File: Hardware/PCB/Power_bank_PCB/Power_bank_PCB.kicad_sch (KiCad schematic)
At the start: 96 parts, among them IC1 TPS63070RNMR, IC2 TPS63070RNMR, J1 Alterative_charging, J2 Vout, Q1 2N7002, Q2 8205A, Q3 2N7002, Q4 2N7002, Q5 2N7002, Q6 DMP3099L, U1 TP4056-42-ESOP8, U2 MCP4018-10k, U3 DW01A, U4 TPS61022, U5 STM32U031F8Px, U6 INA219AxD

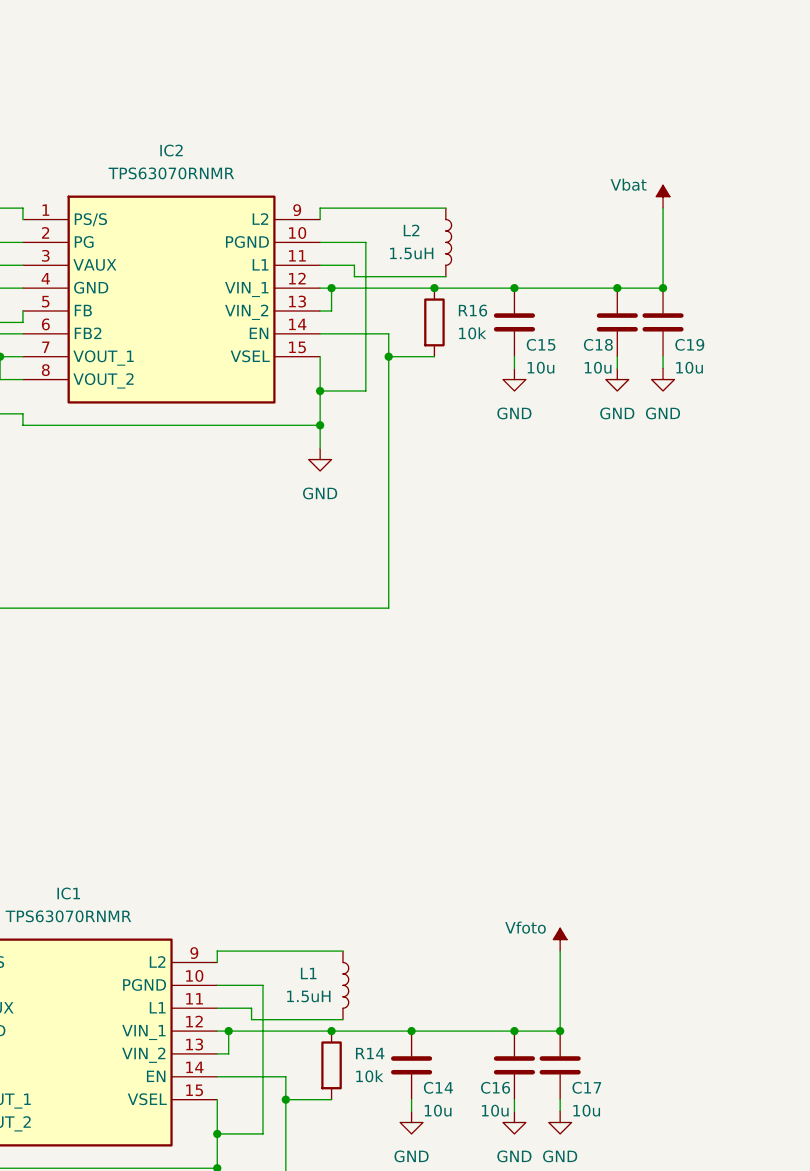
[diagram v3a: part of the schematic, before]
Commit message: First layout without traces
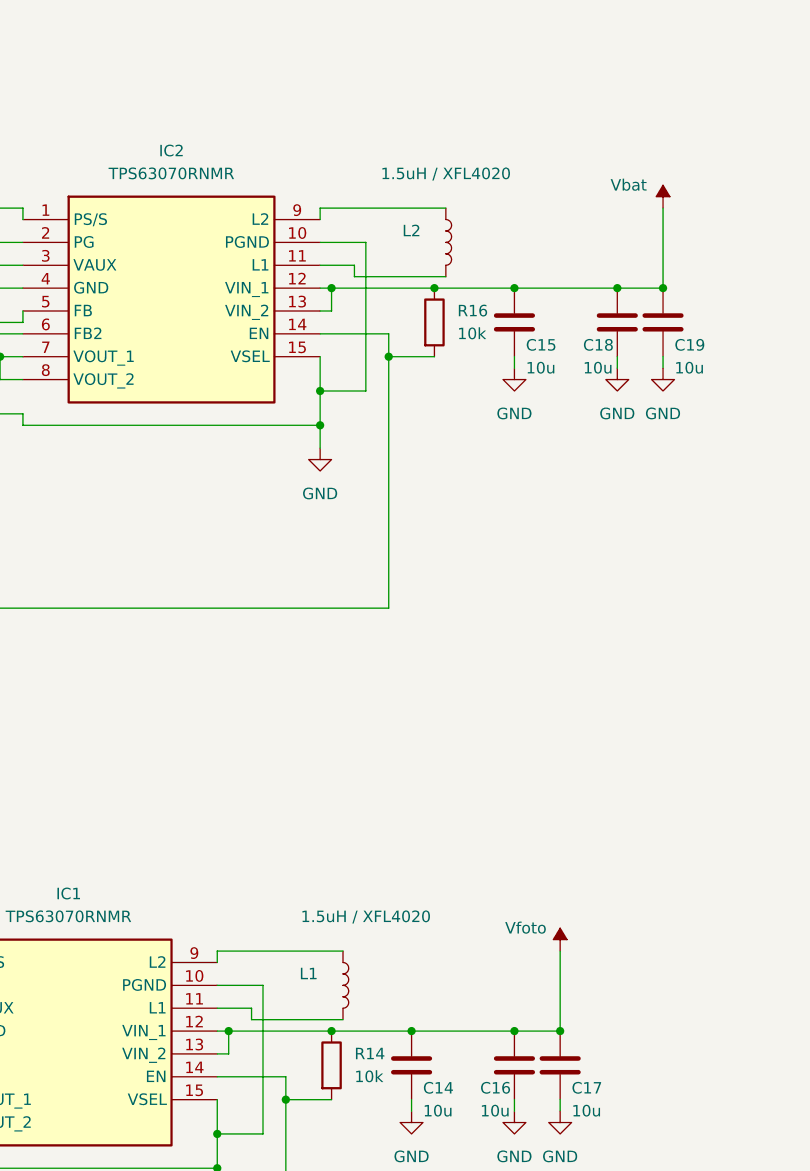
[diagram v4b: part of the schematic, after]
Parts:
- L1, L2: value 1.5uH -> 1.5uH / XFL4020; footprint (none) -> Inductor_SMD:L_Coilcraft_XAL4020-XXX
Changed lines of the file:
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@@
 			)
 		)
-		(property "Value" "1.5uH"
-			(at 139.7 153.67 0)
-			(show_name no)
-			(do_not_autoplace no)
-			(effects
-				(font
-					(size 1.27 1.27)
-				)
-			)
-		)
-		(property "Footprint" ""
+		(property "Value" "1.5uH / XFL4020"
+			(at 143.51 144.78 0)
+			(show_name no)
+			(do_not_autoplace no)
+			(effects
+				(font
+					(size 1.27 1.27)
+				)
+			)
+		)
+		(property "Footprint" "Inductor_SMD:L_Coilcraft_XAL4020-XXX"
 			(at 143.51 152.4 0)
 			(hide yes)
@@
 			)
 		)
-		(property "Value" "1.5uH"
-			(at 128.27 236.22 0)
-			(show_name no)
-			(do_not_autoplace no)
-			(effects
-				(font
-					(size 1.27 1.27)
-				)
-			)
-		)
-		(property "Footprint" ""
+		(property "Value" "1.5uH / XFL4020"
+			(at 134.62 227.33 0)
+			(show_name no)
+			(do_not_autoplace no)
+			(effects
+				(font
+					(size 1.27 1.27)
+				)
+			)
+		)
+		(property "Footprint" "Inductor_SMD:L_Coilcraft_XAL4020-XXX"
 			(at 132.08 234.95 0)
 			(hide yes)

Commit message: Positioned modules on PCB and created zones
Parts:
- TP1, TP10, TP11, TP12, TP2, TP3, TP4, TP5, TP6, TP7, TP8, TP9: footprint TestPoint:TestPoint_Pad_D4.0mm -> TestPoint:TestPoint_Pad_D2.0mm
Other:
- company: (none) -> Bart Soul
- title: (none) -> SolarBank
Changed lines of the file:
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@@
 	(generator_version "10.0")
 	(paper "A3")
+	(title_block
+		(title "SolarBank")
+		(date "2026-09-06")
+		(rev "V1")
+		(company "Bart Soul")
+		(comment 1 "Bartłomiej Dusza")
+	)
 	(junction
 		(at 287.02 121.92)
@@
 			)
 		)
-		(property "Footprint" "TestPoint:TestPoint_Pad_D4.0mm"
+		(property "Footprint" "TestPoint:TestPoint_Pad_D2.0mm"
 			(at 367.03 66.04 0)
 			(hide yes)
@@
 			)
 		)
-		(property "Footprint" "TestPoint:TestPoint_Pad_D4.0mm"
+		(property "Footprint" "TestPoint:TestPoint_Pad_D2.0mm"
 			(at 181.61 58.42 0)
 			(hide yes)
@@
 			)
 		)
-		(property "Footprint" "TestPoint:TestPoint_Pad_D4.0mm"
+		(property "Footprint" "TestPoint:TestPoint_Pad_D2.0mm"
 			(at 335.28 102.87 0)
 			(hide yes)
@@
 			)
 		)
-		(property "Footprint" "TestPoint:TestPoint_Pad_D4.0mm"
+		(property "Footprint" "TestPoint:TestPoint_Pad_D2.0mm"
 			(at 381 71.12 0)
 			(hide yes)
@@
 			)
 		)
-		(property "Footprint" "TestPoint:TestPoint_Pad_D4.0mm"
+		(property "Footprint" "TestPoint:TestPoint_Pad_D2.0mm"
 			(at 364.49 78.74 0)
 			(hide yes)
@@
 			)
 		)
-		(property "Footprint" "TestPoint:TestPoint_Pad_D4.0mm"
+		(property "Footprint" "TestPoint:TestPoint_Pad_D2.0mm"
 			(at 137.16 96.52 0)
 			(hide yes)
@@
 			)
 		)
-		(property "Footprint" "TestPoint:TestPoint_Pad_D4.0mm"
+		(property "Footprint" "TestPoint:TestPoint_Pad_D2.0mm"
 			(at 316.23 177.8 0)
 			(hide yes)
@@
 			)
 		)
-		(property "Footprint" "TestPoint:TestPoint_Pad_D4.0mm"
+		(property "Footprint" "TestPoint:TestPoint_Pad_D2.0mm"
 			(at 335.28 96.52 0)
 			(hide yes)
@@
 			)
 		)
-		(property "Footprint" "TestPoint:TestPoint_Pad_D4.0mm"
+		(property "Footprint" "TestPoint:TestPoint_Pad_D2.0mm"
 			(at 364.49 81.28 0)
 			(hide yes)
@@
 			)
 		)
-		(property "Footprint" "TestPoint:TestPoint_Pad_D4.0mm"
+		(property "Footprint" "TestPoint:TestPoint_Pad_D2.0mm"
 			(at 300.99 60.96 0)
 			(hide yes)
@@
 			)
 		)
-		(property "Footprint" "TestPoint:TestPoint_Pad_D4.0mm"
+		(property "Footprint" "TestPoint:TestPoint_Pad_D2.0mm"
 			(at 381 68.58 0)
 			(hide yes)
@@
 			)
 		)
-		(property "Footprint" "TestPoint:TestPoint_Pad_D4.0mm"
+		(property "Footprint" "TestPoint:TestPoint_Pad_D2.0mm"
 			(at 316.23 180.34 0)
 			(hide yes)

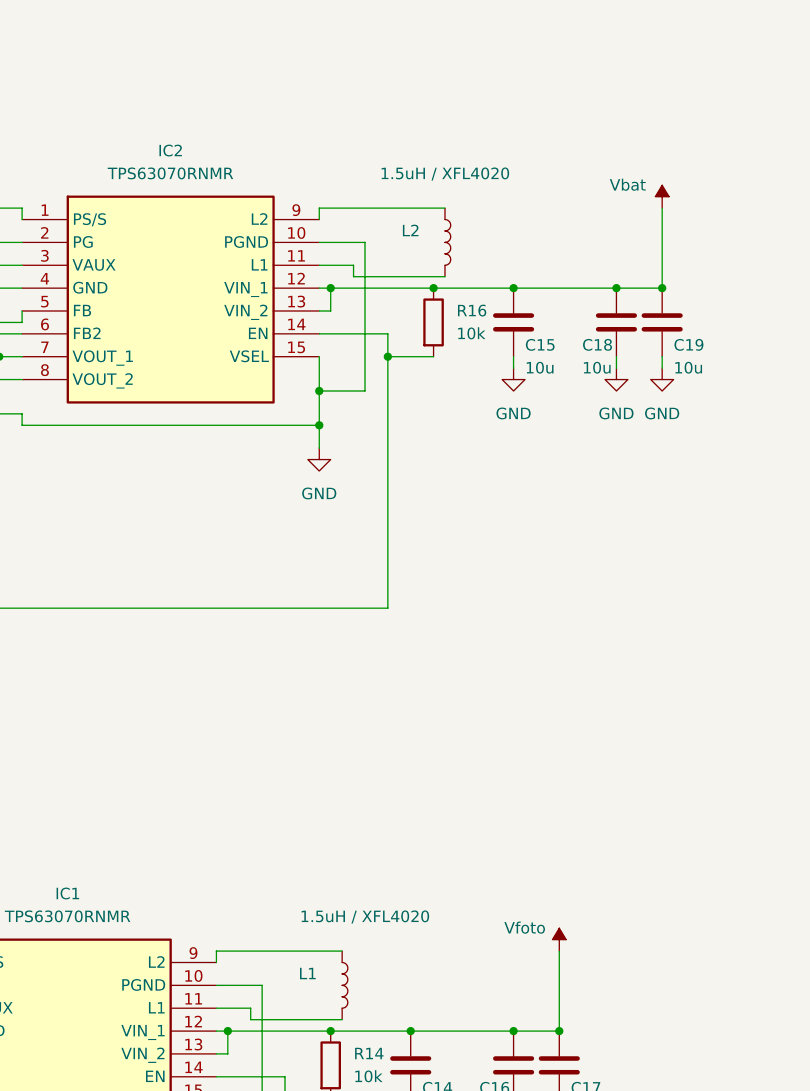
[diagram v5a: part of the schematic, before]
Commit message: Added missing SLT files and added logos
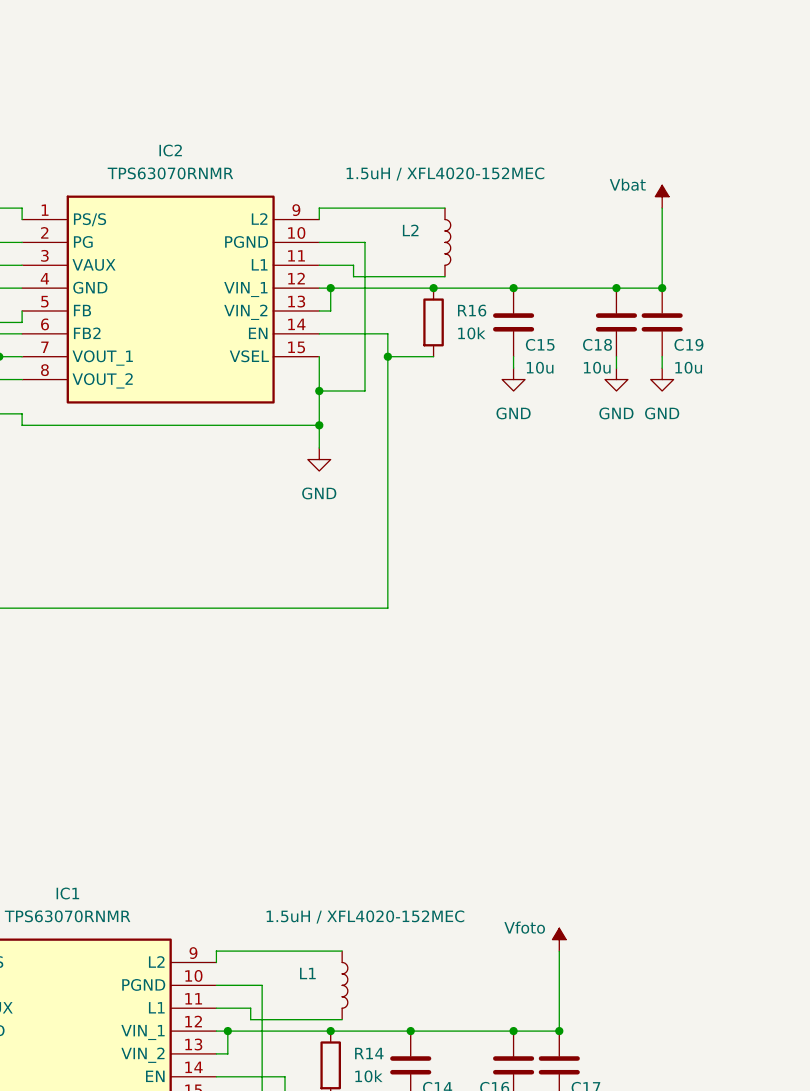
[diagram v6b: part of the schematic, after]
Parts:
- L1, L2: value 1.5uH / XFL4020 -> 1.5uH / XFL4020-152MEC
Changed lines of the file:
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@@
 			)
 		)
-		(property "Value" "1.5uH / XFL4020"
+		(property "Value" "1.5uH / XFL4020-152MEC"
 			(at 143.51 144.78 0)
 			(show_name no)
@@
 			)
 		)
-		(property "Value" "1.5uH / XFL4020"
+		(property "Value" "1.5uH / XFL4020-152MEC"
 			(at 134.62 227.33 0)
 			(show_name no)
